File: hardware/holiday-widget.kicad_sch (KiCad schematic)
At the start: 7 parts, among them J1 I2C, J2 UART, J3 SPI, J33 Conn_02x05_Odd_Even, J4 BATTERY POWER, J5 VDC POWER

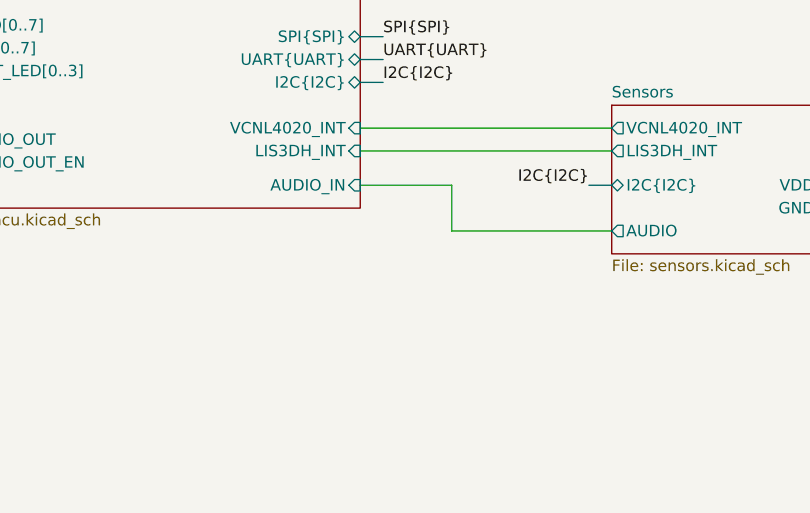
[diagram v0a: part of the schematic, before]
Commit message: [Hardware] Add amplifier to microphone output.
The STM32 part we are using does not include an internal opamp, so we are adding an external opamp to bias and amplify the audio signal.

* Add opamp opa355
* calculate resistor network for gain of 10
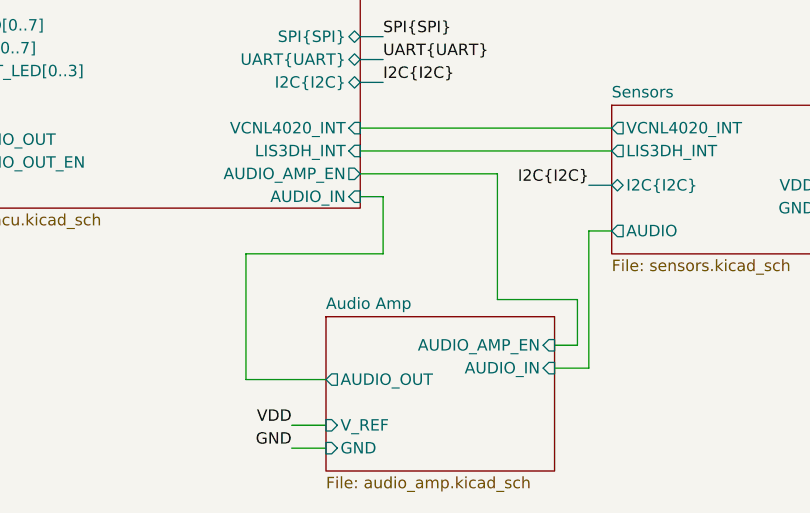
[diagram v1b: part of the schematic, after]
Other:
- added sheet Audio Amp (audio_amp.kicad_sch)
- sheet mcu ports: added AUDIO_AMP_EN; removed none
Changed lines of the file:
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@@
-	(wire
-		(pts
-			(xy 156.21 118.11) (xy 166.37 118.11)
-		)
-		(stroke
-			(width 0)
-			(type default)
-		)
-	)
 	(wire
 		(pts
@@
 	(wire
 		(pts
+			(xy 152.4 139.7) (xy 143.51 139.7)
+		)
+		(stroke
+			(width 0)
+			(type default)
+		)
+	)
+	(wire
+		(pts
 			(xy 106.68 92.71) (xy 110.49 92.71)
 		)
@@
 	(wire
 		(pts
+			(xy 156.21 116.84) (xy 171.45 116.84)
+		)
+		(stroke
+			(width 0)
+			(type default)
+		)
+	)
+	(wire
+		(pts
+			(xy 171.45 130.81) (xy 180.34 130.81)
+		)
+		(stroke
+			(width 0)
+			(type default)
+		)
+	)
+	(wire
+		(pts
 			(xy 168.91 60.96) (xy 170.18 60.96)
 		)
@@
 	(wire
 		(pts
+			(xy 180.34 135.89) (xy 177.8 135.89)
+		)
+		(stroke
+			(width 0)
+			(type default)
+		)
+	)
+	(wire
+		(pts
 			(xy 111.76 53.34) (xy 114.3 53.34)
 		)
@@
 	(wire
 		(pts
+			(xy 184.15 123.19) (xy 181.61 123.19)
+		)
+		(stroke
+			(width 0)
+			(type default)
+		)
+	)
+	(wire
+		(pts
 			(xy 179.07 63.5) (xy 179.07 66.04)
 		)
@@
 	(wire
 		(pts
+			(xy 180.34 130.81) (xy 180.34 135.89)
+		)
+		(stroke
+			(width 0)
+			(type default)
+		)
+	)
+	(wire
+		(pts
 			(xy 200.66 95.25) (xy 156.21 95.25)
 		)
@@
 	(wire
 		(pts
-			(xy 166.37 123.19) (xy 184.15 123.19)
-		)
-		(stroke
-			(width 0)
-			(type default)
-		)
-	)
-	(wire
-		(pts
 			(xy 111.76 58.42) (xy 114.3 58.42)
 		)
@@
 	(wire
 		(pts
+			(xy 143.51 139.7) (xy 143.51 125.73)
+		)
+		(stroke
+			(width 0)
+			(type default)
+		)
+	)
+	(wire
+		(pts
+			(xy 148.59 144.78) (xy 152.4 144.78)
+		)
+		(stroke
+			(width 0)
+			(type default)
+		)
+	)
+	(wire
+		(pts
 			(xy 195.58 71.12) (xy 195.58 90.17)
 		)
@@
 	(wire
 		(pts
+			(xy 143.51 125.73) (xy 158.75 125.73)
+		)
+		(stroke
+			(width 0)
+			(type default)
+		)
+	)
+	(wire
+		(pts
+			(xy 171.45 116.84) (xy 171.45 130.81)
+		)
+		(stroke
+			(width 0)
+			(type default)
+		)
+	)
+	(wire
+		(pts
 			(xy 106.68 90.17) (xy 110.49 90.17)
 		)
@@
 	(wire
 		(pts
+			(xy 181.61 138.43) (xy 177.8 138.43)
+		)
+		(stroke
+			(width 0)
+			(type default)
+		)
+	)
+	(wire
+		(pts
 			(xy 156.21 92.71) (xy 198.12 92.71)
 		)
@@
 	(wire
 		(pts
+			(xy 158.75 125.73) (xy 158.75 119.38)
+		)
+		(stroke
+			(width 0)
+			(type default)
+		)
+	)
+	(wire
+		(pts
 			(xy 156.21 111.76) (xy 184.15 111.76)
 		)
@@
 	(wire
 		(pts
+			(xy 158.75 119.38) (xy 156.21 119.38)
+		)
+		(stroke
+			(width 0)
+			(type default)
+		)
+	)
+	(wire
+		(pts
 			(xy 182.88 63.5) (xy 179.07 63.5)
 		)
@@
 	(wire
 		(pts
-			(xy 166.37 118.11) (xy 166.37 123.19)
+			(xy 181.61 123.19) (xy 181.61 138.43)
 		)
 		(stroke
@@
 		(pts
 			(xy 195.58 90.17) (xy 156.21 90.17)
+		)
+		(stroke
+			(width 0)
+			(type default)
+		)
+	)
+	(wire
+		(pts
+			(xy 148.59 147.32) (xy 152.4 147.32)
 		)
 		(stroke
@@
 		)
 	)
+	(label "GND"
+		(at 148.59 147.32 180)
+		(fields_autoplaced yes)
+		(effects
+			(font
+				(size 1.27 1.27)
+			)
+			(justify right bottom)
+		)
+	)
 	(label "SPI.DIN"
 		(at 247.65 129.54 180)
@@
 	(label "GND"
 		(at 57.15 55.88 180)
+		(fields_autoplaced yes)
+		(effects
+			(font
+				(size 1.27 1.27)
+			)
+			(justify right bottom)
+		)
+	)
+	(label "VDD"
+		(at 148.59 144.78 180)
 		(fields_autoplaced yes)
 		(effects
@@
 		)
 		(pin "AUDIO_IN" input
-			(at 156.21 118.11 0)
+			(at 156.21 119.38 0)
 			(effects
 				(font
@@
 		(pin "nRST" input
 			(at 156.21 90.17 0)
+			(effects
+				(font
+					(size 1.27 1.27)
+				)
+				(justify right)
+			)
+		)
+		(pin "AUDIO_AMP_EN" output
+			(at 156.21 116.84 0)
 			(effects
 				(font
@@
 				)
 			)
+		)
+	)
+	(sheet
+		(at 152.4 132.715)
+		(size 25.4 17.145)
+		(fields_autoplaced yes)
+		(stroke
+			(width 0.1524)
+			(type solid)
+		)
+		(fill
+			(color 0 0 0 0.0000)
+		)
+		(property "Sheetname" "Audio Amp"
+			(at 152.4 132.0034 0)
+			(effects
+				(font
+					(size 1.27 1.27)
+				)
+				(justify left bottom)
+			)
+		)
+		(property "Sheetfile" "audio_amp.kicad_sch"
+			(at 152.4 150.4446 0)
+			(effects
+				(font
+					(size 1.27 1.27)
+				)
+				(justify left top)
+			)
+		)
+		(pin "AUDIO_OUT" output
+			(at 152.4 139.7 180)
+			(effects
+				(font
+					(size 1.27 1.27)
+				)
+				(justify left)
+			)
+		)
+		(pin "V_REF" input
+			(at 152.4 144.78 180)
+			(effects
+				(font
+					(size 1.27 1.27)
+				)
+				(justify left)
+			)
+		)
+		(pin "GND" input
+			(at 152.4 147.32 180)
+			(effects
+				(font
+					(size 1.27 1.27)
+				)
+				(justify left)
+			)
+		)
+		(pin "AUDIO_AMP_EN" input
+			(at 177.8 135.89 0)
+			(effects
+				(font
+					(size 1.27 1.27)
+				)
+				(justify right)
+			)
+		)
+		(pin "AUDIO_IN" input
+			(at 177.8 138.43 0)
+			(effects
+				(font
+					(size 1.27 1.27)
+				)
+				(justify right)
+			)
+		)
+		(instances
+			(project "holiday-widget"
+				(path "/addc3208-a9c4-4d28-9808-559c1d81e43b"
+					(page "8")
+				)
+			)

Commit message: [Hardware] Remove unused breakouts
* Remove extra GPIO and SPI outputs from MCU
* remove auxillary connectors for GPIO, SPI, and I2C
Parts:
- removed J1: I2C, Connector_PinHeader_1.27mm:PinHeader_1x04_P1.27mm_Vertical, symbol Connector_Generic:Conn_01x04
- removed J3: SPI, Connector_PinHeader_1.27mm:PinHeader_1x05_P1.27mm_Vertical, symbol Connector_Generic:Conn_01x05
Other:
- sheet Input and Output ports: added none; removed GPIO[0..7]
- sheet mcu ports: added none; removed GPIO[0..7], SPI{SPI}

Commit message: [Hardware] Resize UART header to be 2.54mm pitch.
Previous revision had incorrectly sized pinout, correct this.
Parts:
- J2: footprint Connector_PinHeader_1.27mm:PinHeader_1x04_P1.27mm_Vertical -> Connector_PinHeader_2.54mm:PinHeader_1x04_P2.54mm_Vertical
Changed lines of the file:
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@@
 			)
 		)
-		(property "Footprint" "Connector_PinHeader_1.27mm:PinHeader_1x04_P1.27mm_Vertical"
+		(property "Footprint" "Connector_PinHeader_2.54mm:PinHeader_1x04_P2.54mm_Vertical"
 			(at 252.73 100.33 0)
 			(effects

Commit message: [Hardware] Update LEDs
Add additional LEDs and arrange in 7x7 matrix. Remove 2x status LEDs. Reroute MCU connetions to be more sensible. Rearrange components.
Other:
- sheet Input and Output ports: added LED_CTRL[0..13], STAT_LED[0..1]; removed LED_CTRL[0..7], STAT_LED[0..3]
- sheet mcu ports: added LED[0..13], STAT_LED[0..1]; removed LED[0..7], STAT_LED[0..3]
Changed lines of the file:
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@@
 			)
 		)
-		(pin "LED_CTRL[0..7]" input
+		(pin "LED_CTRL[0..13]" input
 			(at 85.09 102.87 0)
 			(effects
@@
 			)
 		)
-		(pin "STAT_LED[0..3]" input
+		(pin "STAT_LED[0..1]" input
 			(at 85.09 105.41 0)
 			(effects
@@
 			)
 		)
-		(pin "LED[0..7]" output
+		(pin "LED[0..13]" output
 			(at 110.49 102.87 180)
 			(effects
@@
 			)
 		)
-		(pin "STAT_LED[0..3]" output
+		(pin "STAT_LED[0..1]" output
 			(at 110.49 105.41 180)
 			(effects

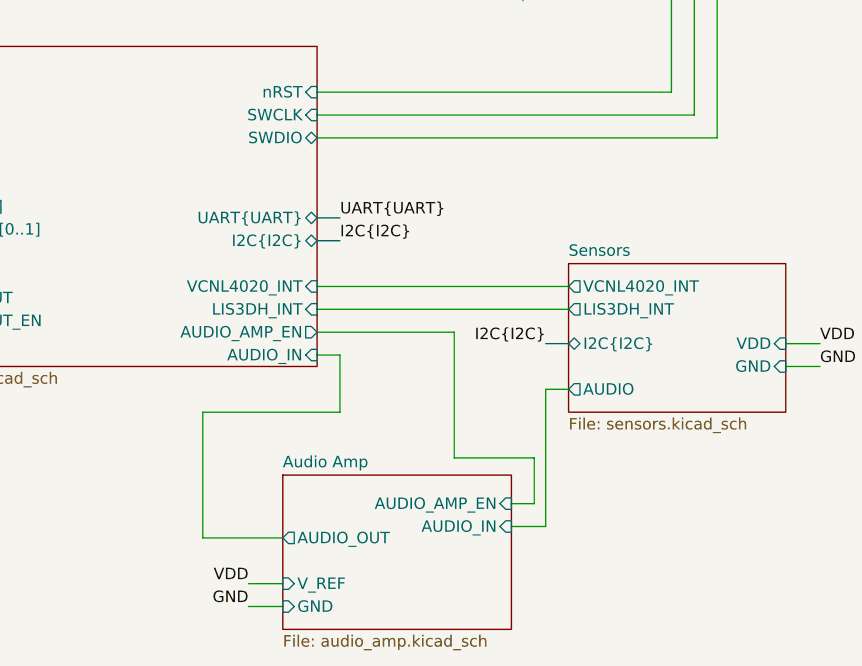
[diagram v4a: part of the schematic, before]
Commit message: [Hardware] Replace LISDH Motion Sensor with LSM6DSM
Change motion sensor to an accelerometer + gyro unit. Route the second interrupt line to the STM32.
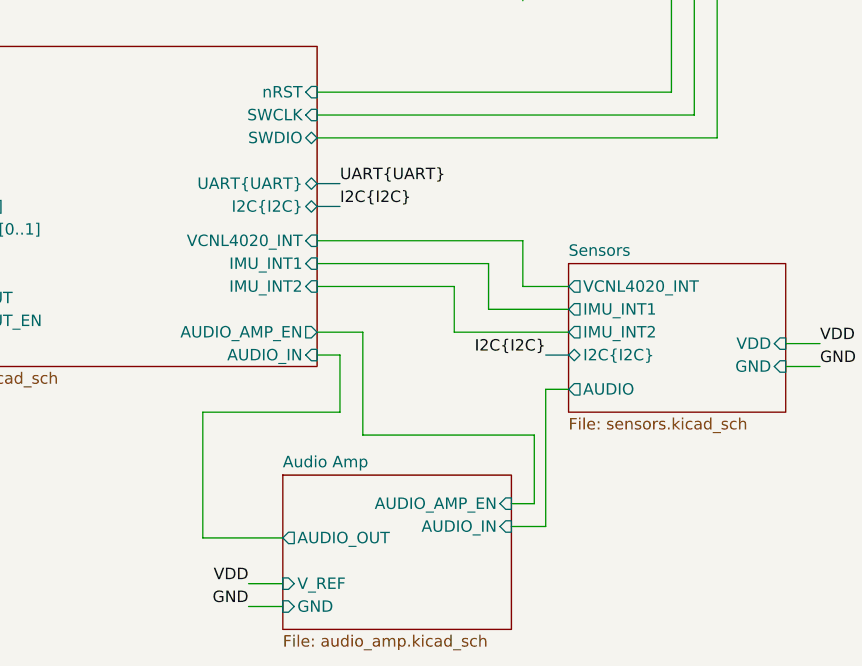
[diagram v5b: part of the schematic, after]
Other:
- sheet Sensors ports: added IMU_INT1, IMU_INT2; removed LIS3DH_INT
- sheet mcu ports: added IMU_INT1, IMU_INT2; removed LIS3DH_INT
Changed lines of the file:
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@@
+		)
+	)
+	(wire
+		(pts
+			(xy 175.26 109.22) (xy 175.26 114.3)
+		)
+		(stroke
+			(width 0)
+			(type default)
 		)
 	)
 	(bus
 		(pts
-			(xy 156.21 104.14) (xy 158.75 104.14)
+			(xy 156.21 100.33) (xy 158.75 100.33)
 		)
 		(stroke
@@
 	(wire
 		(pts
+			(xy 156.21 116.84) (xy 161.29 116.84)
+		)
+		(stroke
+			(width 0)
+			(type default)
+		)
+	)
+	(wire
+		(pts
+			(xy 171.45 111.76) (xy 171.45 116.84)
+		)
+		(stroke
+			(width 0)
+			(type default)
+		)
+	)
+	(wire
+		(pts
 			(xy 106.68 92.71) (xy 110.49 92.71)
 		)
@@
 	(wire
 		(pts
-			(xy 156.21 116.84) (xy 171.45 116.84)
-		)
-		(stroke
-			(width 0)
-			(type default)
-		)
-	)
-	(wire
-		(pts
-			(xy 171.45 130.81) (xy 180.34 130.81)
+			(xy 161.29 116.84) (xy 161.29 128.27)
+		)
+		(stroke
+			(width 0)
+			(type default)
+		)
+	)
+	(wire
+		(pts
+			(xy 161.29 128.27) (xy 180.34 128.27)
 		)
 		(stroke
@@
 	(wire
 		(pts
+			(xy 171.45 116.84) (xy 184.15 116.84)
+		)
+		(stroke
+			(width 0)
+			(type default)
+		)
+	)
+	(wire
+		(pts
 			(xy 180.34 135.89) (xy 177.8 135.89)
 		)
@@
 	(wire
 		(pts
-			(xy 180.34 130.81) (xy 180.34 135.89)
+			(xy 180.34 128.27) (xy 180.34 135.89)
 		)
 		(stroke
@@
 	(wire
 		(pts
-			(xy 156.21 114.3) (xy 184.15 114.3)
+			(xy 156.21 109.22) (xy 175.26 109.22)
 		)
 		(stroke
@@
 	(wire
 		(pts
-			(xy 171.45 116.84) (xy 171.45 130.81)
-		)
-		(stroke
-			(width 0)
-			(type default)
-		)
-	)
-	(wire
-		(pts
 			(xy 106.68 90.17) (xy 110.49 90.17)
 		)
@@
 	(wire
 		(pts
+			(xy 156.21 111.76) (xy 171.45 111.76)
+		)
+		(stroke
+			(width 0)
+			(type default)
+		)
+	)
+	(wire
+		(pts
 			(xy 156.21 92.71) (xy 198.12 92.71)
 		)
@@
 	(wire
 		(pts
+			(xy 175.26 114.3) (xy 184.15 114.3)
+		)
+		(stroke
+			(width 0)
+			(type default)
+		)
+	)
+	(wire
+		(pts
 			(xy 200.66 60.96) (xy 200.66 95.25)
 		)
@@
 	(wire
 		(pts
-			(xy 156.21 111.76) (xy 184.15 111.76)
+			(xy 156.21 106.68) (xy 179.07 106.68)
+		)
+		(stroke
+			(width 0)
+			(type default)
+		)
+	)
+	(wire
+		(pts
+			(xy 179.07 111.76) (xy 184.15 111.76)
 		)
 		(stroke
@@
 	(bus
 		(pts
-			(xy 181.61 118.11) (xy 184.15 118.11)
+			(xy 181.61 119.38) (xy 184.15 119.38)
 		)
 		(stroke
@@
 	(wire
 		(pts
+			(xy 179.07 106.68) (xy 179.07 111.76)
+		)
+		(stroke
+			(width 0)
+			(type default)
+		)
+	)
+	(wire
+		(pts
 			(xy 85.09 113.03) (xy 110.49 113.03)
 		)
@@
 	(bus
 		(pts
-			(xy 156.21 106.68) (xy 158.75 106.68)
+			(xy 156.21 102.87) (xy 158.75 102.87)
 		)
 		(stroke
@@
 	)
 	(label "I2C{I2C}"
-		(at 158.75 106.68 0)
+		(at 158.75 102.87 0)
 		(fields_autoplaced yes)
 		(effects
@@
 	)
 	(label "I2C{I2C}"
-		(at 181.61 118.11 180)
+		(at 181.61 119.38 180)
 		(fields_autoplaced yes)
 		(effects
@@
 	)
 	(label "UART{UART}"
-		(at 158.75 104.14 0)
+		(at 158.75 100.33 0)
 		(fields_autoplaced yes)
 		(effects
@@
 		)
 		(pin "UART{UART}" bidirectional
-			(at 156.21 104.14 0)
+			(at 156.21 100.33 0)
 			(effects
 				(font
@@
 		)
 		(pin "I2C{I2C}" bidirectional
-			(at 156.21 106.68 0)
+			(at 156.21 102.87 0)
 			(effects
 				(font
@@
 		)
 		(pin "VCNL4020_INT" input
-			(at 156.21 111.76 0)
-			(effects
-				(font
-					(size 1.27 1.27)
-				)
-				(justify right)
-			)
-		)
-		(pin "LIS3DH_INT" input
-			(at 156.21 114.3 0)
+			(at 156.21 106.68 0)
 			(effects
 				(font
@@
 		(pin "AUDIO_AMP_EN" output
 			(at 156.21 116.84 0)
+			(effects
+				(font
+					(size 1.27 1.27)
+				)
+				(justify right)
+			)
+		)
+		(pin "IMU_INT1" input
+			(at 156.21 109.22 0)
+			(effects
+				(font
+					(size 1.27 1.27)
+				)
+				(justify right)
+			)
+		)
+		(pin "IMU_INT2" input
+			(at 156.21 111.76 0)
 			(effects
 				(font
@@
 		)
 		(pin "I2C{I2C}" bidirectional
-			(at 184.15 118.11 180)
+			(at 184.15 119.38 180)
 			(effects
 				(font
@@
 			)
 		)
-		(pin "LIS3DH_INT" output
-			(at 184.15 114.3 180)
-			(effects
-				(font
-					(size 1.27 1.27)
-				)
-				(justify left)
-			)
-		)
 		(pin "VDD" input
 			(at 208.28 118.11 0)
@@
 			)
 		)
+		(pin "IMU_INT1" output
+			(at 184.15 114.3 180)
+			(effects
+				(font
+					(size 1.27 1.27)
+				)
+				(justify left)
+			)
+		)
+		(pin "IMU_INT2" output
+			(at 184.15 116.84 180)
+			(effects
+				(font
+					(size 1.27 1.27)
+				)
+				(justify left)
+			)
+		)

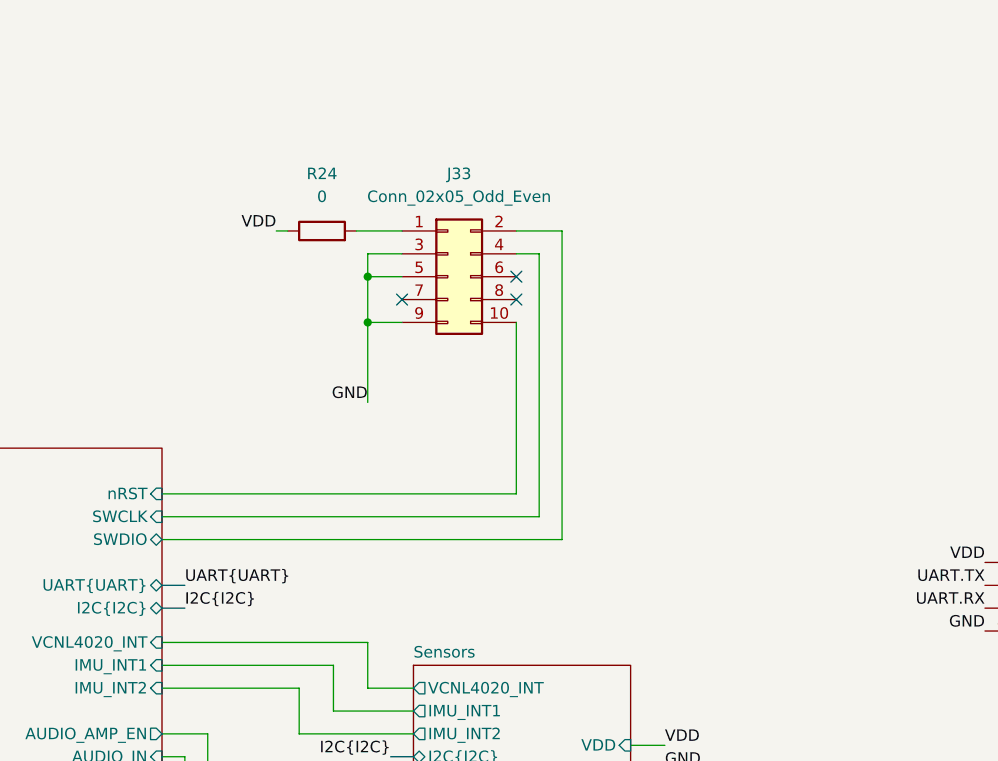
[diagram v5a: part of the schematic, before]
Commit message: [Hardware] Add ferrite bead to VDDA. Swap schematic symbol for SWD-specific one. Add some notes to MCU pins.
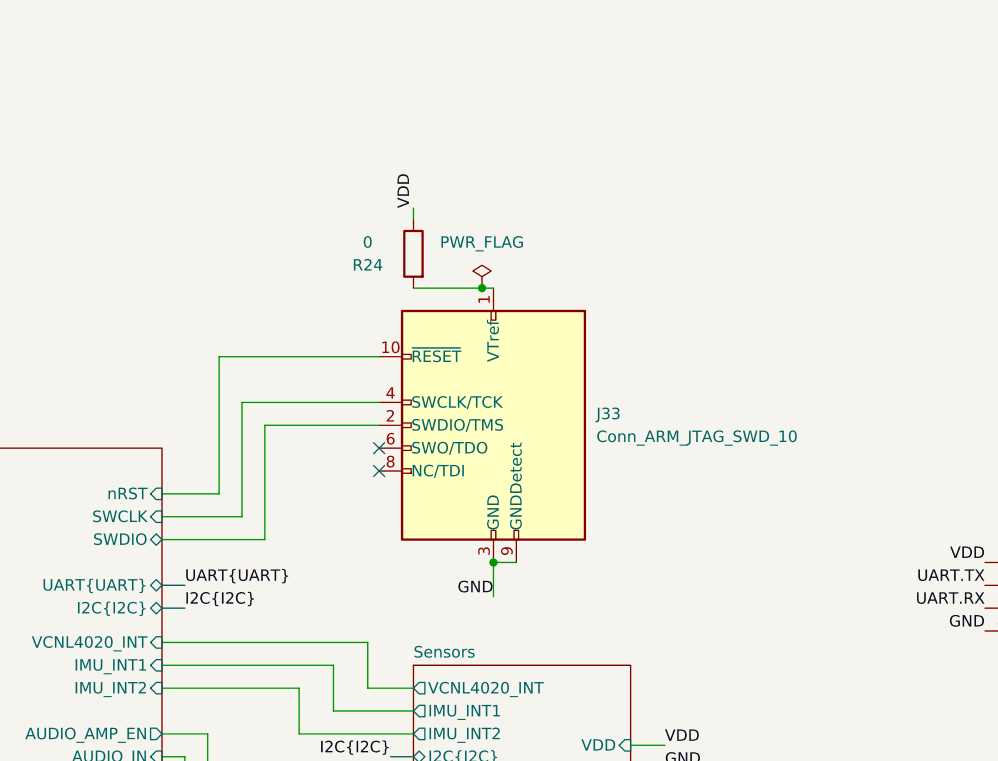
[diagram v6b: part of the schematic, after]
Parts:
- J33: value Conn_02x05_Odd_Even -> Conn_ARM_JTAG_SWD_10; symbol Connector_Generic:Conn_02x05_Odd_Even -> Connector:Conn_ARM_JTAG_SWD_10
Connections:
- no-connect marks 3 -> 2
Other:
- moved on the sheet: R24

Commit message: Change many passives to 0402 and assign part numbers
Incorporate 0402 parts where possible
Assign Manufacturer Part Numbers to parts where possible
Update layout for the new passive sizes
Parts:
- R24: footprint Resistor_SMD:R_0603_1608Metric_Pad0.98x0.95mm_HandSolder -> Resistor_SMD:R_0402_1005Metric; MPN (none) -> RC0402JR-070RL
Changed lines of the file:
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@@
+			)
+		)
+		(property "MPN" ""
+			(at 193.04 82.55 0)
+			(effects
+				(font
+					(size 1.27 1.27)
+				)
+				(hide yes)
 			)
 		)
@@
 			)
 		)
+		(property "MPN" ""
+			(at 62.23 29.21 0)
+			(effects
+				(font
+					(size 1.27 1.27)
+				)
+				(hide yes)
+			)
+		)
 		(pin "2"
 		)
@@
 			)
 		)
-		(property "Footprint" "Resistor_SMD:R_0603_1608Metric_Pad0.98x0.95mm_HandSolder"
+		(property "Footprint" "Resistor_SMD:R_0402_1005Metric"
 			(at 185.928 63.5 90)
 			(effects
@@
 		)
 		(property "Description" "Resistor"
+			(at 184.15 63.5 0)
+			(effects
+				(font
+					(size 1.27 1.27)
+				)
+				(hide yes)
+			)
+		)
+		(property "MPN" "RC0402JR-070RL"
 			(at 184.15 63.5 0)
 			(effects
@@
 			)
 		)
+		(property "MPN" ""
+			(at 252.73 100.33 0)
+			(effects
+				(font
+					(size 1.27 1.27)
+				)
+				(hide yes)
+			)
+		)
 		(pin "1"
 		)
@@
 			(at 62.23 53.34 0)
 			(effects
+				(font
+					(size 1.27 1.27)
+				)
+				(hide yes)
+			)
+		)
+		(property "MPN" ""
+			(at 62.23 53.34 0)
+			(effects
